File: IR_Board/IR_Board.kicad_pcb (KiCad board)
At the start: 2 copper layers, 16 parts, among them J1 Conn_02x08_Row_Letter_First, U1 TSSP58038, U10 TSSP58038, U11 TSSP58038, U12 TSSP58038, U13 TSSP58038, U14 TSSP58038, U2 TSSP58038, U3 TSSP58038, U4 TSSP58038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

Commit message: Started IR PCB
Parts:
- added C10: 220n, Capacitor_SMD:C_0603_1608Metric, F.Cu at (166.3, 98.2)
- added C11: 220n, Capacitor_SMD:C_0603_1608Metric, F.Cu at (162.3, 102.1)
- added C12: 220n, Capacitor_SMD:C_0603_1608Metric, F.Cu at (169.4, 95.7)
- added C13: 220n, Capacitor_SMD:C_0603_1608Metric, F.Cu at (150.3, 112.6)
- added C14: 220n, Capacitor_SMD:C_0603_1608Metric, F.Cu at (158.1, 104.9)
- added C15: 220n, Capacitor_SMD:C_0603_1608Metric, F.Cu at (146.3, 116.6)
- added C2: 220n, Capacitor_SMD:C_0603_1608Metric, F.Cu at (151.3, 147.6)
- added C3: 220n, Capacitor_SMD:C_0603_1608Metric, F.Cu at (162.1, 107.4)
- added C4: 220n, Capacitor_SMD:C_0603_1608Metric, F.Cu at (154.3, 113.8)
- added C5: 220n, Capacitor_SMD:C_0603_1608Metric, F.Cu at (166.3, 100.8)
- added C6: 220n, Capacitor_SMD:C_0603_1608Metric, F.Cu at (154.3, 111.2)
- added C7: 220n, Capacitor_SMD:C_0603_1608Metric, F.Cu at (162.1, 104.9)
- added C8: 220n, Capacitor_SMD:C_0603_1608Metric, F.Cu at (158.1, 107.4)
- added C9: 220n, Capacitor_SMD:C_0603_1608Metric, F.Cu at (150.3, 115.1)
- added D1: B, LED_SMD:LED_0805_2012Metric_Pad1.15x1.40mm_HandSolder, F.Cu at (124.9, 113.7)
- added D2: A, LED_SMD:LED_0805_2012Metric_Pad1.15x1.40mm_HandSolder, F.Cu at (129.6, 94.2)
- added Q1: FDG6335N, Package_TO_SOT_SMD:SOT-363_SC-70-6, F.Cu at (151.4, 151.4)
- added Q10: FDG6335N, Package_TO_SOT_SMD:SOT-363_SC-70-6, F.Cu at (145.7, 110.9)
- added Q11: FDG6335N, Package_TO_SOT_SMD:SOT-363_SC-70-6, F.Cu at (137.9, 114.7)
- added Q12: FDG6335N, Package_TO_SOT_SMD:SOT-363_SC-70-6, F.Cu at (150.0, 104.4)
- added Q13: FDG6335N, Package_TO_SOT_SMD:SOT-363_SC-70-6, F.Cu at (142.1, 114.7)
- added Q14: FDG6335N, Package_TO_SOT_SMD:SOT-363_SC-70-6, F.Cu at (129.4, 114.1)
- added Q2: FDG6335N, Package_TO_SOT_SMD:SOT-363_SC-70-6, F.Cu at (133.6, 113.5)
- added Q3: FDG6335N, Package_TO_SOT_SMD:SOT-363_SC-70-6, F.Cu at (141.5, 107.0)
- added Q4: FDG6335N, Package_TO_SOT_SMD:SOT-363_SC-70-6, F.Cu at (149.9, 100.5)
- added Q5: FDG6335N, Package_TO_SOT_SMD:SOT-363_SC-70-6, F.Cu at (145.7, 107.0)
- added Q6: FDG6335N, Package_TO_SOT_SMD:SOT-363_SC-70-6, F.Cu at (141.5, 110.9)
- added Q7: FDG6335N, Package_TO_SOT_SMD:SOT-363_SC-70-6, F.Cu at (165.8, 87.5)
- added Q8: FDG6335N, Package_TO_SOT_SMD:SOT-363_SC-70-6, F.Cu at (161.5, 91.4)
- added Q9: FDG6335N, Package_TO_SOT_SMD:SOT-363_SC-70-6, F.Cu at (154.1, 100.5)
- added R1: 10k, Resistor_SMD:R_0603_1608Metric, F.Cu at (162.3, 99.6)
- added R10: 10k, Resistor_SMD:R_0603_1608Metric, F.Cu at (161.4, 97.1)
- added R11: 10k, Resistor_SMD:R_0603_1608Metric, F.Cu at (149.8, 110.1)
- added R12: 10k, Resistor_SMD:R_0603_1608Metric, F.Cu at (146.3, 114.1)
- added R13: 10k, Resistor_SMD:R_0603_1608Metric, F.Cu at (154.1, 106.2)
- added R14: 10k, Resistor_SMD:R_0603_1608Metric, F.Cu at (165.4, 95.7)
- added R15: 10k, Resistor_SMD:R_0603_1608Metric, F.Cu at (158.3, 102.4)
- added R16: 10k, Resistor_SMD:R_0603_1608Metric, F.Cu at (153.9, 108.7)
- added R17: 10k, Resistor_SMD:R_0603_1608Metric, F.Cu at (129.1, 97.0)
- added R2: 10k, Resistor_SMD:R_0603_1608Metric, F.Cu at (151.3, 149.1)
- added R3: 10k, Resistor_SMD:R_0603_1608Metric, F.Cu at (124.1, 116.6)
- added R4: 10k, Resistor_SMD:R_0603_1608Metric, F.Cu at (161.4, 94.6)
- added R5: 10k, Resistor_SMD:R_0603_1608Metric, F.Cu at (165.6, 90.7)
- added R6: 10k, Resistor_SMD:R_0603_1608Metric, F.Cu at (149.8, 107.6)
- added R7: 10k, Resistor_SMD:R_0603_1608Metric, F.Cu at (158.3, 99.9)
- added R8: 10k, Resistor_SMD:R_0603_1608Metric, F.Cu at (154.1, 103.7)
- added R9: 10k, Resistor_SMD:R_0603_1608Metric, F.Cu at (165.6, 93.2)
- added SW1: SW_SPDT, Main_Board:EG1218, B.Cu at (131.7, 158.6)
- C1: footprint Capacitor_SMD:C_0603_1608Metric_Pad1.05x0.95mm_HandSolder -> Capacitor_SMD:C_0603_1608Metric
- J1: value Conn_02x08_Row_Letter_First -> Conn_02x08_Top_Bottom; footprint Connector_JST:JST_PHD_B16B-PHDSS_2x08_P2.00mm_Vertical -> Connector_Hirose:Hirose_DF11-16DP-2DSA_2x08_P2.00mm_Vertical
- moved U13 192.6 mm to (217.8, 166.0), turned to 51.4 degrees
- moved U12 182.1 mm to (235.5, 131.6), turned to 77.1 degrees
- moved U11 171.6 mm to (236.7, 93.0), turned to 102.9 degrees
- moved U14 162.8 mm to (183.9, 163.4)
- moved U1 160.7 mm to (148.9, 163.4)
- moved U10 160.0 mm to (220.9, 57.7), turned to 128.6 degrees
- moved J1 154.7 mm to (157.9, 142.0), turned to 180 degrees
- moved U9 140.3 mm to (191.4, 32.7), turned to 154.3 degrees
- moved U2 138.1 mm to (113.9, 163.4)
- moved U3 124.1 mm to (82.0, 162.1), turned to 308.6 degrees
- moved C1 122.4 mm to (123.7, 128.0), turned to 0 degrees
- moved U4 81.8 mm to (66.2, 126.7), turned to 282.9 degrees
- moved U8 81.6 mm to (153.9, 23.1), turned to 180 degrees
- moved U7 75.5 mm to (116.0, 30.5), turned to 205.7 degrees
- moved U5 47.4 mm to (67.4, 88.1), turned to 257.1 degrees
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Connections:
- C1 pad 1: +5V -> +3V3
- U1 pad 1: Net-(J1-Padb2) -> Net-(Q1-Pad3)
- U1 pad 3: +5V -> +3V3
- U10 pad 1: Net-(J1-Pada6) -> Net-(Q10-Pad3)
- U10 pad 3: +5V -> +3V3
- U11 pad 1: Net-(J1-Pada5) -> Net-(Q11-Pad3)
- U11 pad 3: +5V -> +3V3
- U12 pad 1: Net-(J1-Pada4) -> Net-(Q12-Pad3)
- U12 pad 3: +5V -> +3V3
- U13 pad 1: Net-(J1-Pada3) -> Net-(Q13-Pad3)
- U13 pad 3: +5V -> +3V3
- U14 pad 1: Net-(J1-Pada2) -> Net-(Q14-Pad3)
- U14 pad 3: +5V -> +3V3
- U2 pad 1: Net-(J1-Padb3) -> Net-(Q2-Pad3)
- U2 pad 3: +5V -> +3V3
- U3 pad 1: Net-(J1-Padb4) -> Net-(Q3-Pad3)
- U3 pad 3: +5V -> +3V3
- U4 pad 1: Net-(J1-Padb5) -> Net-(Q4-Pad3)
- U4 pad 3: +5V -> +3V3
- U5 pad 1: Net-(J1-Padb6) -> Net-(Q5-Pad3)
- U5 pad 3: +5V -> +3V3
- U6 pad 1: Net-(J1-Padb7) -> Net-(Q6-Pad3)
- U6 pad 3: +5V -> +3V3
- U7 pad 1: Net-(J1-Padb8) -> Net-(Q7-Pad3)
- U7 pad 3: +5V -> +3V3
- U8 pad 1: Net-(J1-Pada8) -> Net-(Q8-Pad3)
- U8 pad 3: +5V -> +3V3
- U9 pad 1: Net-(J1-Pada7) -> Net-(Q9-Pad3)
- U9 pad 3: +5V -> +3V3
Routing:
- net Net-(Q1-Pad4): track 0.00 -> 3.64 mm
- net Net-(C2-Pad2): track 0.00 -> 1.54 mm
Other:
- board outline added: 189.9 x 157.6 mm

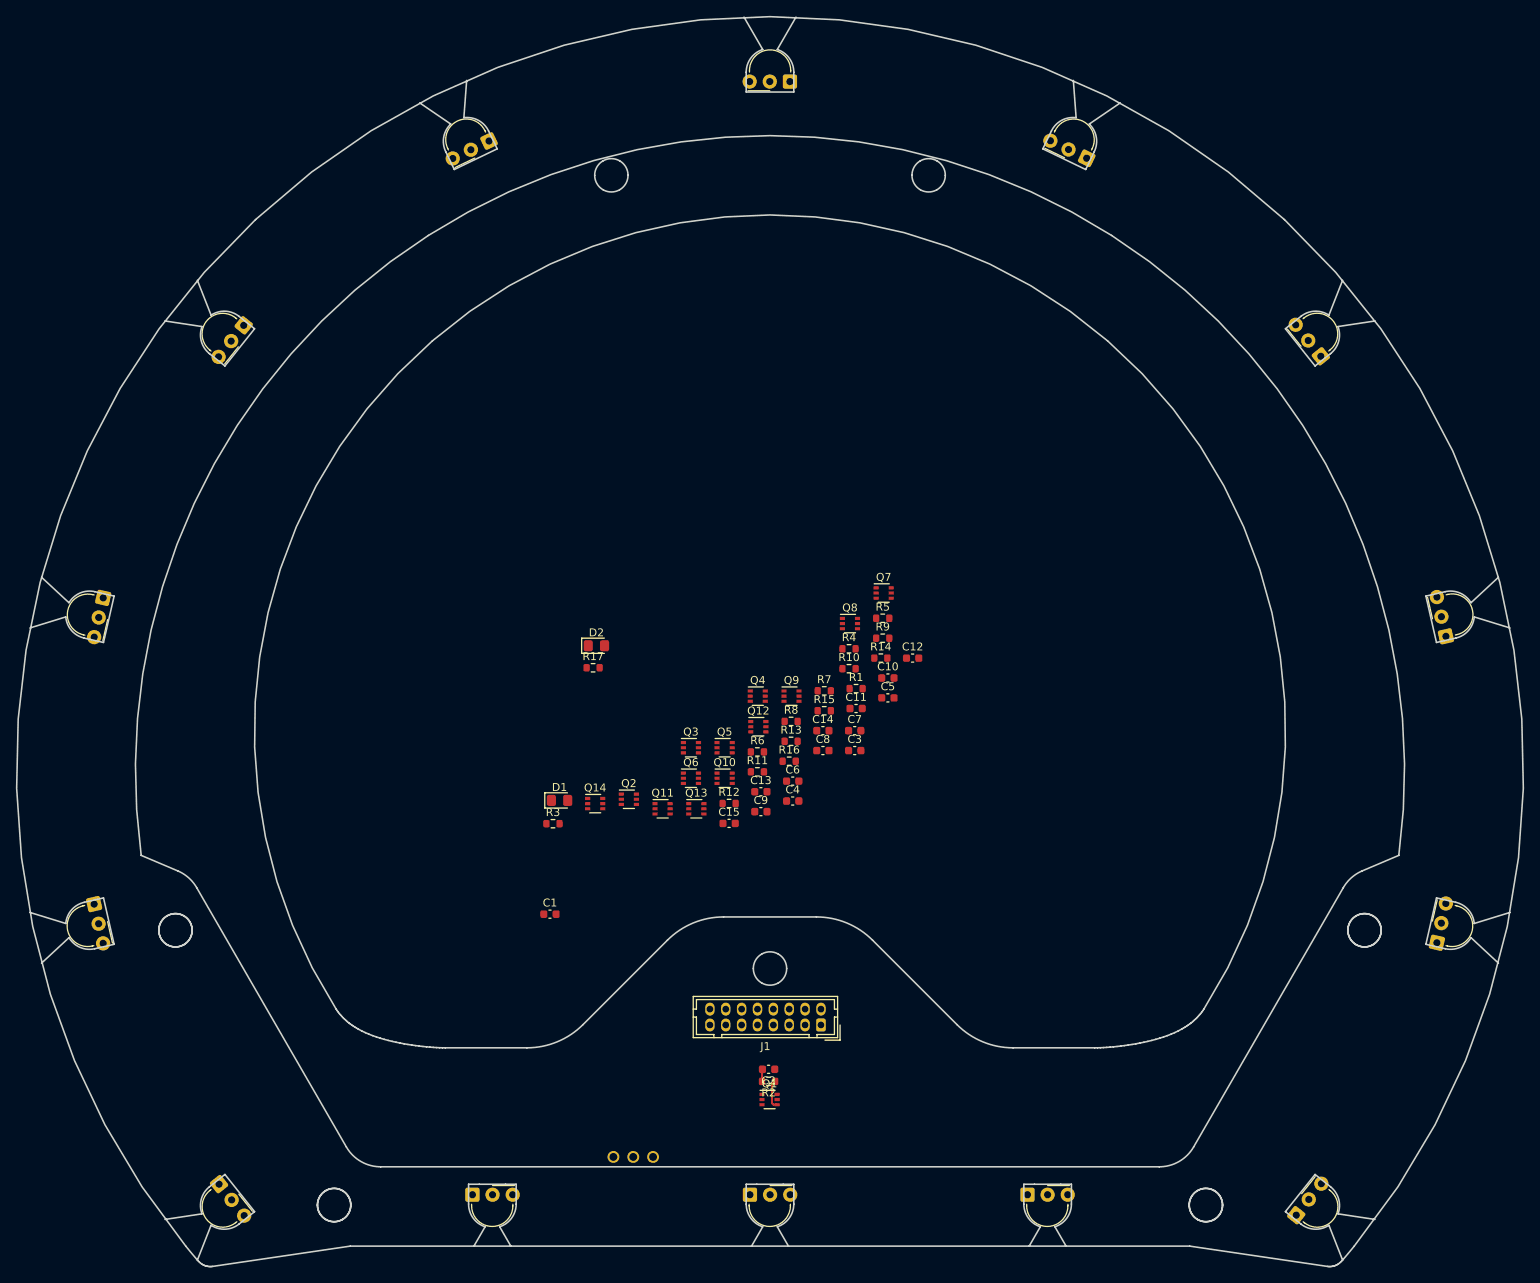
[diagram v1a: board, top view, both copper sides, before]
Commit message: Updated to Kicad 6
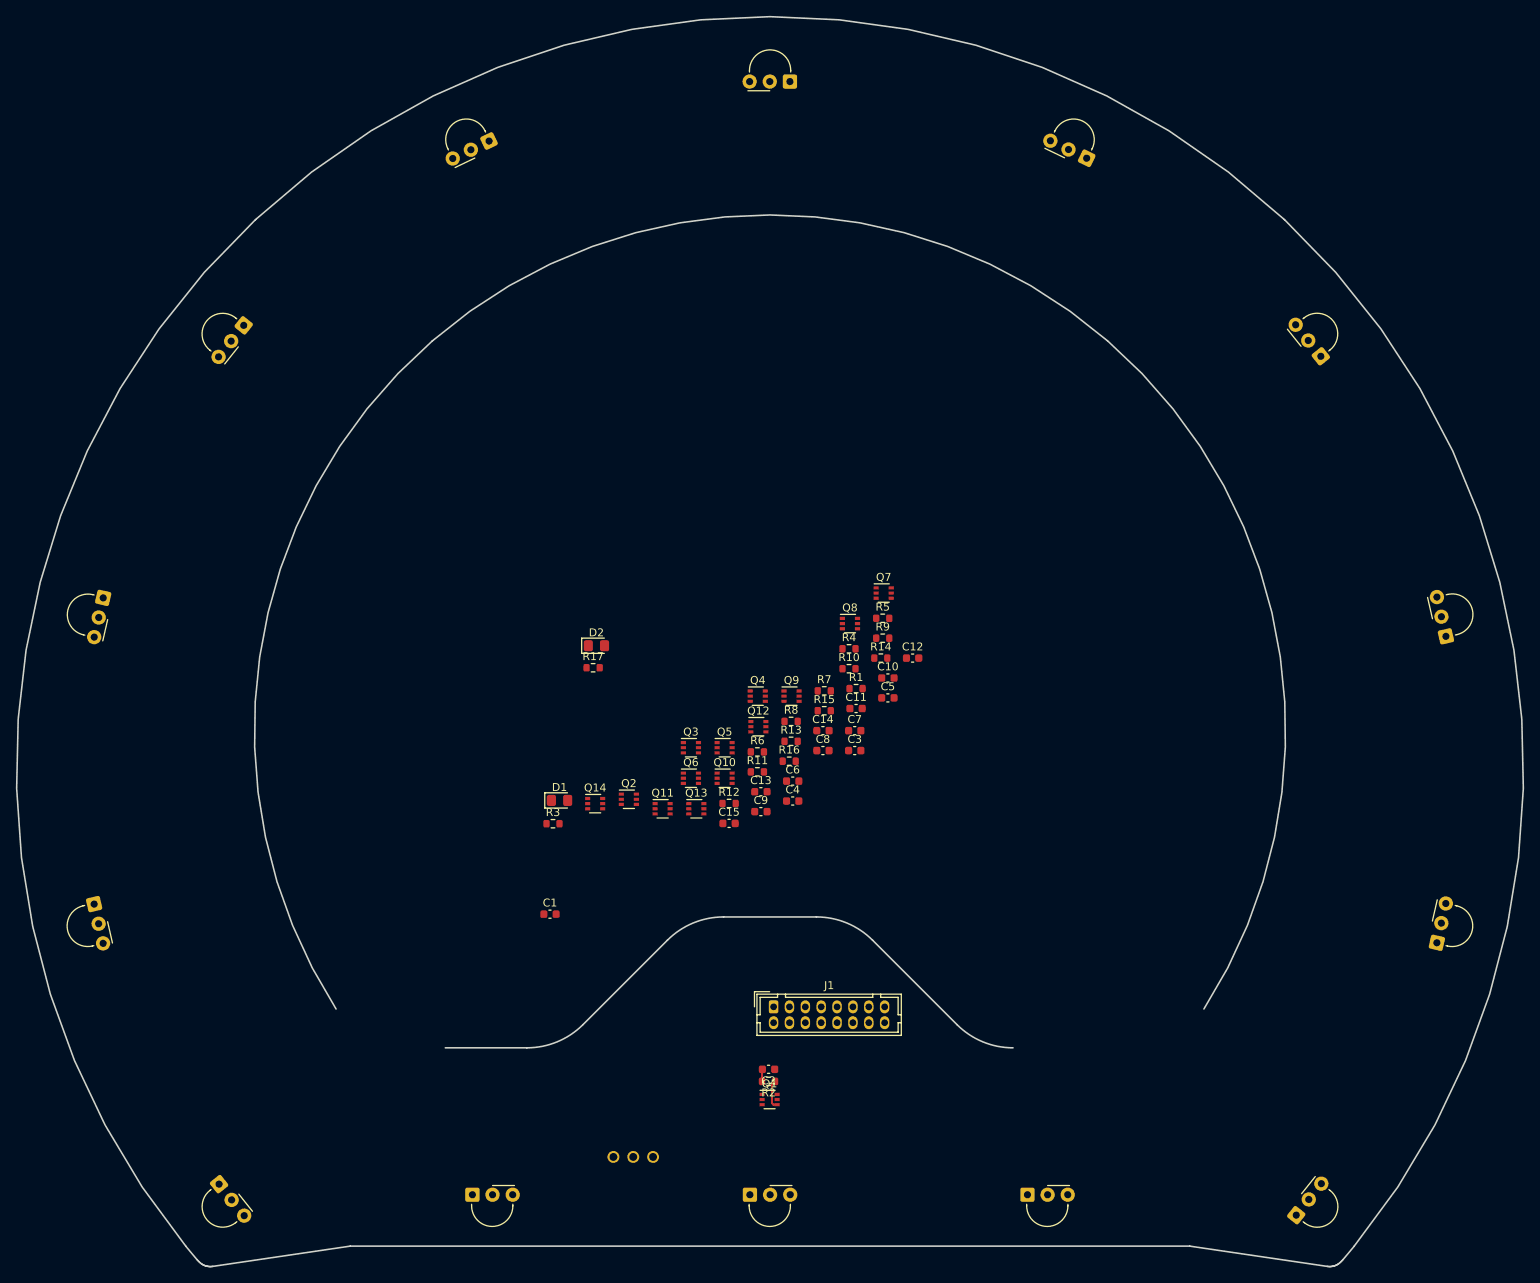
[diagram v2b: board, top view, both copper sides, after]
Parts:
- moved J1 6.39 mm to (151.9, 139.7), turned to 0 degrees
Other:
- outline, holes or cut-outs redrawn
- net class Default removed
